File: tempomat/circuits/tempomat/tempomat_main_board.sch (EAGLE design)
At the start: 43 parts, among them Q1 2N4033, T1 TIP122, T2 TIP122, T3 TIP32, T3-TIP127 BDX54, T4-TIP127 BDX54, U2 LM747N, U4_XOR- 4070N, U5-LM2931 78L05Z

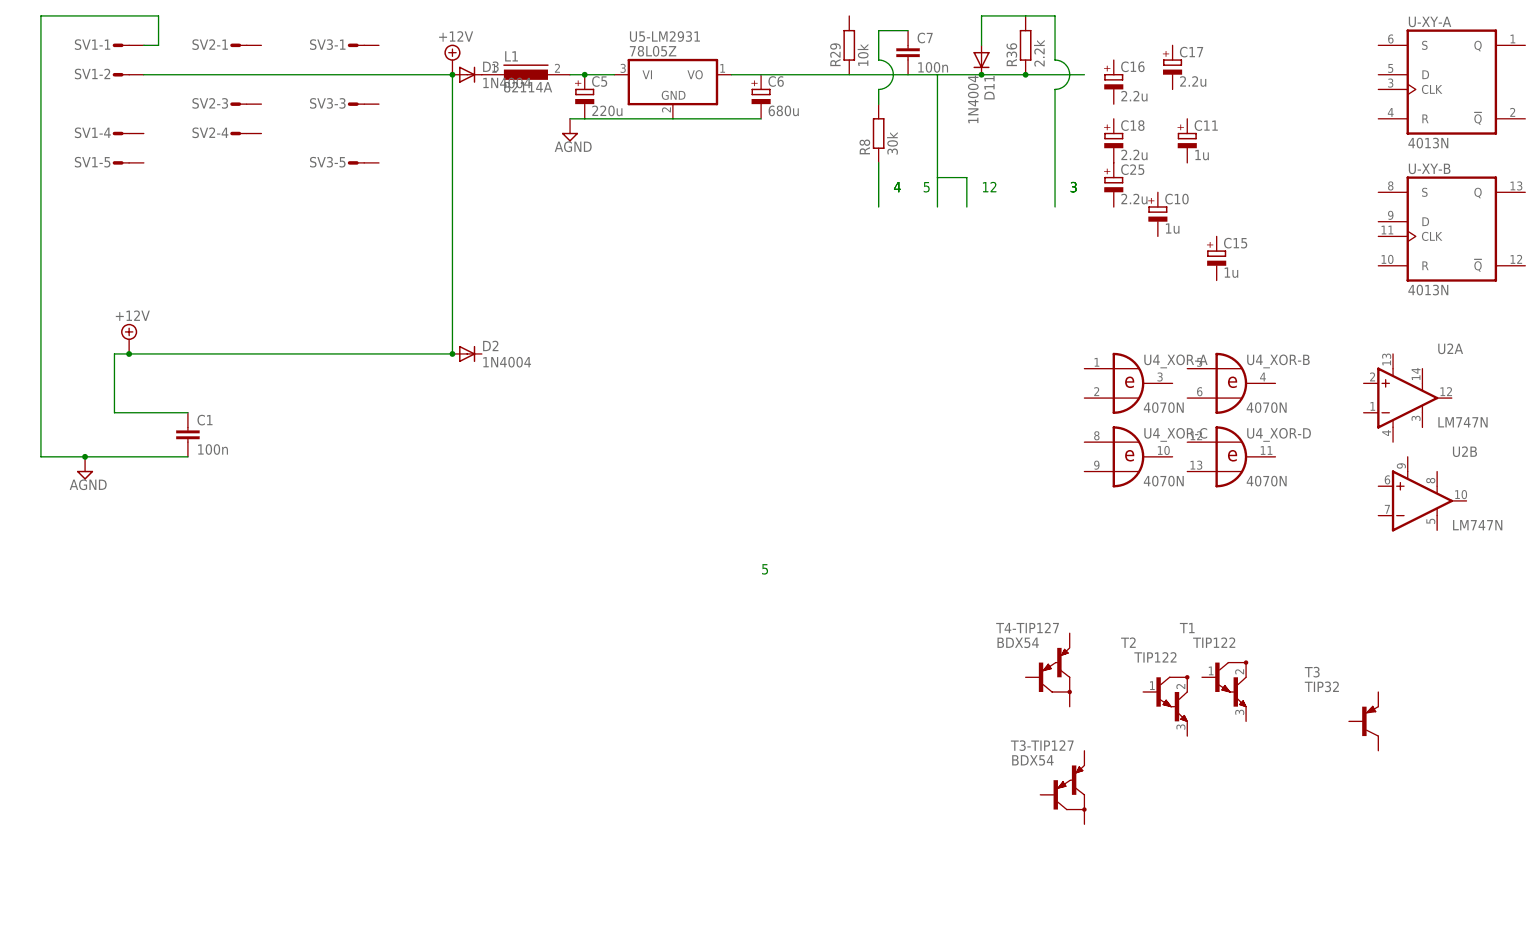
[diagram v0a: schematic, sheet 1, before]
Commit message: repairing tempomat
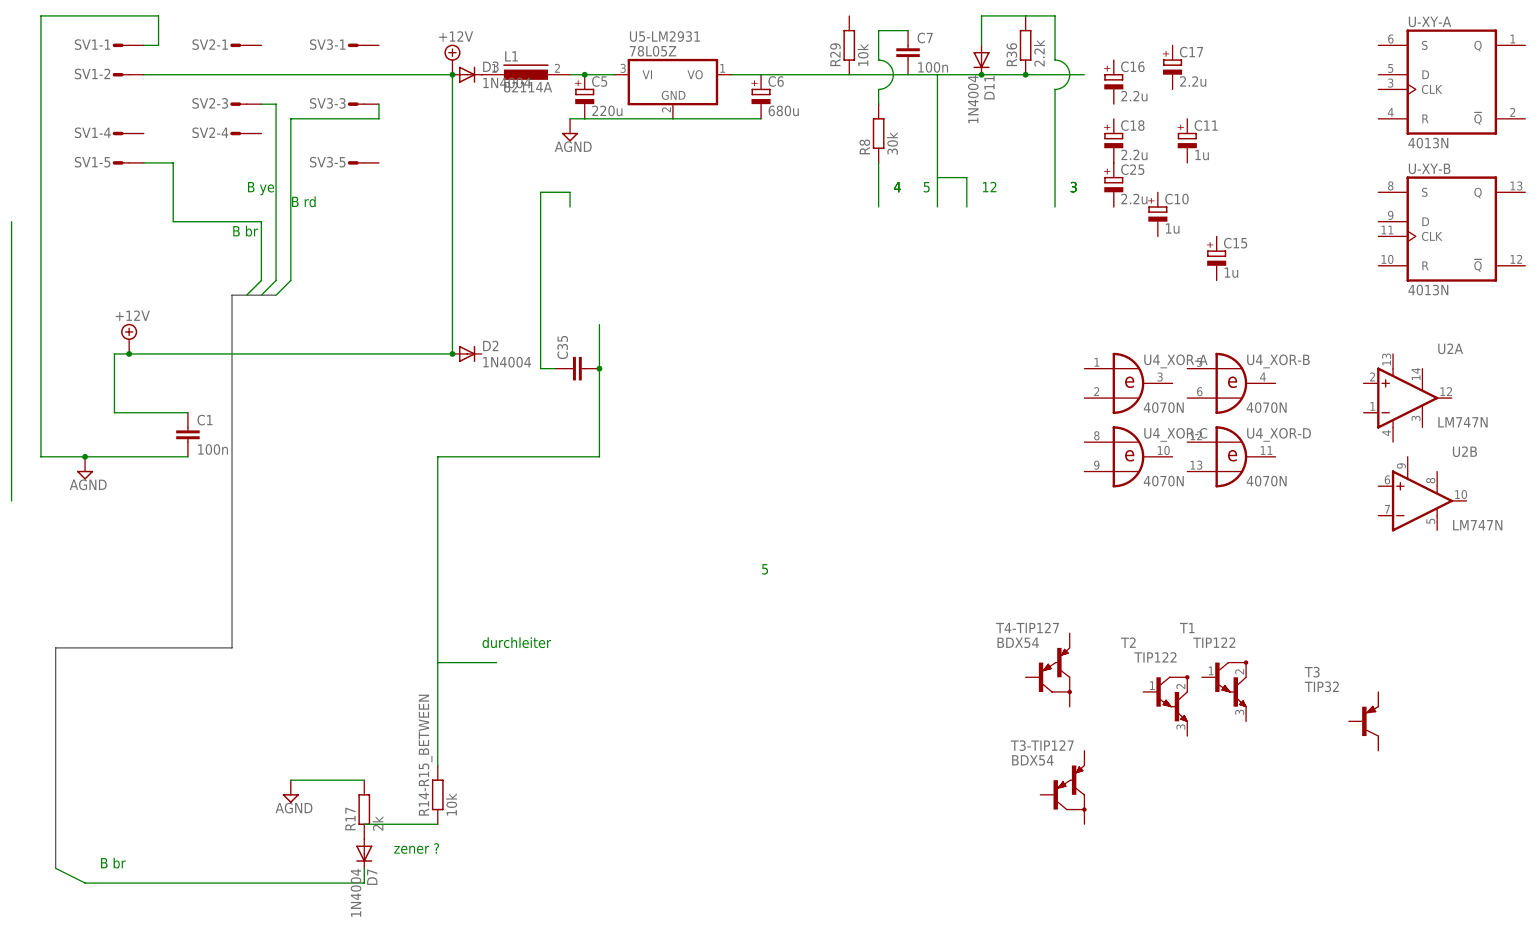
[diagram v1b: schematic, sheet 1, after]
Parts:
- added C35: (no value), resistor:C-EU025_050-045X075
- added D7: 1N4004, diode:1N4004
- added R14-R15_BETWEEN: 10k, resistor:R-EU_0204/2V
- added R17: 2k, resistor:R-EU_0204/2V
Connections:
- new net N$19: SV1-5.S
- new net N$20: SV3-3.S
- new net N$21: D7.C
- new net N$22: D7.A, R17.1
- new net N$23: R14-R15_BETWEEN.1
- new net N$24: C35.1
- new net N$25: C35.2, R14-R15_BETWEEN.2
- new net N$8: SV2-3.S
- net AGND: now also R17.2
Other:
- note added: "B br"
- note added: "B rd"
- note added: "B ye"
- note added: "durchleiter"
- note added: "what for this pnp ?"
- note added: "zener ?"
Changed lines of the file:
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@@
 <part name="Q1" library="transistor-pnp" deviceset="2N4033*" device=""/>
 <part name="R4" library="resistor" deviceset="R-EU_" device="0207/7" value="4.7k"/>
+<part name="D7" library="diode" deviceset="1N4004" device=""/>
+<part name="R17" library="resistor" deviceset="R-EU_" device="0204/2V" value="2k"/>
+<part name="SUPPLY7" library="supply2" deviceset="AGND" device=""/>
+<part name="R14-R15_BETWEEN" library="resistor" deviceset="R-EU_" device="0204/2V" value="10k"/>
+<part name="C35" library="resistor" deviceset="C-EU" device="025_050-045X075"/>
 </parts>
 <sheets>
@@
 <text x="144.78" y="71.12" size="1.778" layer="91">3</text>
 <text x="144.78" y="71.12" size="1.778" layer="91">3</text>
+<text x="0" y="63.5" size="1.778" layer="91">B br</text>
+<text x="2.54" y="71.12" size="1.778" layer="91">B ye</text>
+<text x="10.16" y="68.58" size="1.778" layer="91">B rd</text>
+<text x="-22.86" y="-45.72" size="1.778" layer="91">B br</text>
+<text x="27.94" y="-43.18" size="1.778" layer="91">zener ?</text>
+<text x="43.18" y="-7.62" size="1.778" layer="91">durchleiter</text>
 </plain>
 <instances>
@@
 <instance part="R36" gate="G$1" x="137.16" y="96.52" rot="R90"/>
 <instance part="R8" gate="G$1" x="111.76" y="81.28" rot="R90"/>
+<instance part="D7" gate="1" x="22.86" y="-43.18" rot="R270"/>
+<instance part="R17" gate="G$1" x="22.86" y="-35.56" rot="R90"/>
+<instance part="SUPPLY7" gate="G$1" x="10.16" y="-33.02"/>
+<instance part="R14-R15_BETWEEN" gate="G$1" x="35.56" y="-33.02" rot="R90"/>
+<instance part="C35" gate="G$1" x="58.42" y="40.64" rot="R90"/>
 </instances>
 <busses>
+<bus name="B$1">
+<segment>
+<wire x1="0" y1="53.34" x2="7.62" y2="53.34" width="0.762" layer="92"/>
+<wire x1="0" y1="53.34" x2="0" y2="-7.62" width="0.762" layer="92"/>
+<wire x1="0" y1="-7.62" x2="-30.48" y2="-7.62" width="0.762" layer="92"/>
+<wire x1="-30.48" y1="-7.62" x2="-30.48" y2="-45.72" width="0.762" layer="92"/>
+</segment>
+</bus>
 </busses>
 <nets>
@@
 <pinref part="C6" gate="G$1" pin="-"/>
 <wire x1="76.2" y1="83.82" x2="91.44" y2="83.82" width="0.1524" layer="91"/>
+</segment>
+<segment>
+<pinref part="R17" gate="G$1" pin="2"/>
+<wire x1="22.86" y1="-30.48" x2="10.16" y2="-30.48" width="0.1524" layer="91"/>
+<pinref part="SUPPLY7" gate="G$1" pin="AGND"/>
 </segment>
 </net>
@@
 </segment>
 </net>
+<net name="N$18" class="0">
+<segment>
+<wire x1="-38.1" y1="66.04" x2="-38.1" y2="17.78" width="0.1524" layer="91"/>
+</segment>
+</net>
+<net name="N$19" class="0">
+<segment>
+<pinref part="SV1" gate="-5" pin="S"/>
+<wire x1="-15.24" y1="76.2" x2="-10.16" y2="76.2" width="0.1524" layer="91"/>
+<wire x1="-10.16" y1="76.2" x2="-10.16" y2="66.04" width="0.1524" layer="91"/>
+<wire x1="-10.16" y1="66.04" x2="5.08" y2="66.04" width="0.1524" layer="91"/>
+<wire x1="5.08" y1="66.04" x2="5.08" y2="55.88" width="0.1524" layer="91"/>
+<wire x1="5.08" y1="55.88" x2="2.54" y2="53.34" width="0.1524" layer="91"/>
+</segment>
+</net>
+<net name="N$8" class="0">
+<segment>
+<pinref part="SV2" gate="-3" pin="S"/>
+<wire x1="5.08" y1="86.36" x2="7.62" y2="86.36" width="0.1524" layer="91"/>
+<wire x1="7.62" y1="86.36" x2="7.62" y2="55.88" width="0.1524" layer="91"/>
+<wire x1="7.62" y1="55.88" x2="5.08" y2="53.34" width="0.1524" layer="91"/>
+</segment>
+</net>
+<net name="N$20" class="0">
+<segment>
+<pinref part="SV3" gate="-3" pin="S"/>
+<wire x1="25.4" y1="86.36" x2="25.4" y2="83.82" width="0.1524" layer="91"/>
+<wire x1="25.4" y1="83.82" x2="10.16" y2="83.82" width="0.1524" layer="91"/>
+<wire x1="10.16" y1="83.82" x2="10.16" y2="55.88" width="0.1524" layer="91"/>
+<wire x1="10.16" y1="55.88" x2="7.62" y2="53.34" width="0.1524" layer="91"/>
+</segment>
+</net>
+<net name="N$21" class="0">
+<segment>
+<wire x1="-30.48" y1="-45.72" x2="-25.4" y2="-48.26" width="0.1524" layer="91"/>
+<wire x1="-25.4" y1="-48.26" x2="22.86" y2="-48.26" width="0.1524" layer="91"/>
+<pinref part="D7" gate="1" pin="C"/>
+<wire x1="22.86" y1="-48.26" x2="22.86" y2="-45.72" width="0.1524" layer="91"/>
+</segment>
+</net>
+<net name="N$22" class="0">
+<segment>
+<pinref part="D7" gate="1" pin="A"/>
+<pinref part="R17" gate="G$1" pin="1"/>
+</segment>
+</net>
+<net name="N$23" class="0">
+<segment>
+<pinref part="R14-R15_BETWEEN" gate="G$1" pin="1"/>
+<wire x1="22.86" y1="-38.1" x2="35.56" y2="-38.1" width="0.1524" layer="91"/>
+</segment>
+</net>
+<net name="N$25" class="0">
+<segment>
+<pinref part="C35" gate="G$1" pin="2"/>
+<wire x1="63.5" y1="40.64" x2="63.5" y2="48.26" width="0.1524" layer="91"/>
+<junction x="63.5" y="40.64"/>
+<pinref part="R14-R15_BETWEEN" gate="G$1" pin="2"/>
+<wire x1="35.56" y1="-27.94" x2="35.56" y2="-10.16" width="0.1524" layer="91"/>
+<wire x1="35.56" y1="-10.16" x2="35.56" y2="25.4" width="0.1524" layer="91"/>
+<wire x1="35.56" y1="25.4" x2="63.5" y2="25.4" width="0.1524" layer="91"/>
+<wire x1="63.5" y1="25.4" x2="63.5" y2="40.64" width="0.1524" layer="91"/>
+<wire x1="35.56" y1="-10.16" x2="45.72" y2="-10.16" width="0.4064" layer="91"/>
+</segment>
+</net>
+<net name="N$24" class="0">
+<segment>
+<pinref part="C35" gate="G$1" pin="1"/>
+<wire x1="55.88" y1="40.64" x2="53.34" y2="40.64" width="0.1524" layer="91"/>
+<wire x1="53.34" y1="40.64" x2="53.34" y2="71.12" width="0.1524" layer="91"/>
+<wire x1="53.34" y1="71.12" x2="58.42" y2="71.12" width="0.1524" layer="91"/>
+<wire x1="58.42" y1="71.12" x2="58.42" y2="68.58" width="0.1524" layer="91"/>
+</segment>
+</net>
 </nets>
 </sheet>
@@
 <text x="53.34" y="40.64" size="1.778" layer="91">on</text>
 <text x="149.86" y="35.56" size="1.778" layer="91">on-off indicator light</text>
+<text x="17.78" y="30.48" size="2.54" layer="91">what for this pnp ?</text>
 </plain>
 <instances>
